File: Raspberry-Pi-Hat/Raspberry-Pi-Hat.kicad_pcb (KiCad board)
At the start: 4 copper layers, 65 x 56 mm, 127 parts, among them J1 Screw_Terminal_01x04, J2 Screw_Terminal_01x02, J3 40HAT, J4 Screw_Terminal_01x02, J5 USB_B, J6 CONN_02X02, J7 USB_A, J8 USB_A, J9 CONN_01X02, Q1 DMG2305UX, Q2 DMMT5401, U1 ADM3490ExR, U2 CAT24C32, U3 TCAN330, U4 LMZ13608, U5 TUSB4041I, U6 MCP2221AxSL, U7 MCP2221AxSL, U8 TPS2561, U9 TPS2561, Y1 24MHz

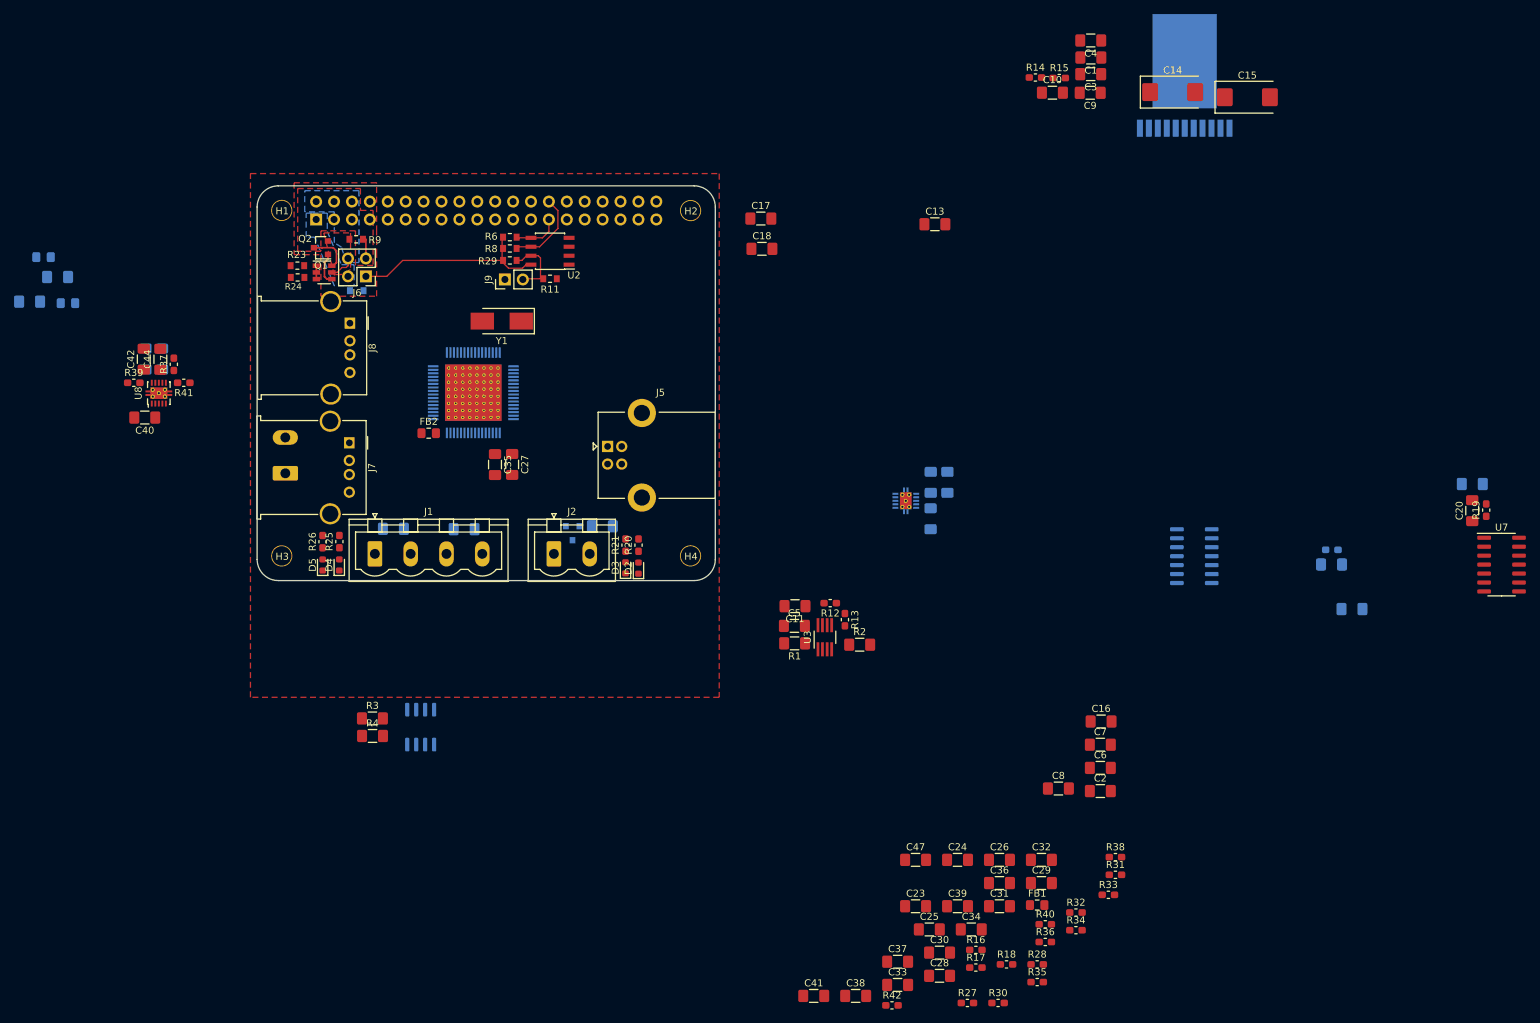
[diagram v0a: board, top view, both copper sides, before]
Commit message: Placed all component on board
All component placed on board.
Not many space left. Will probably reduce size of capacitors and resistors.
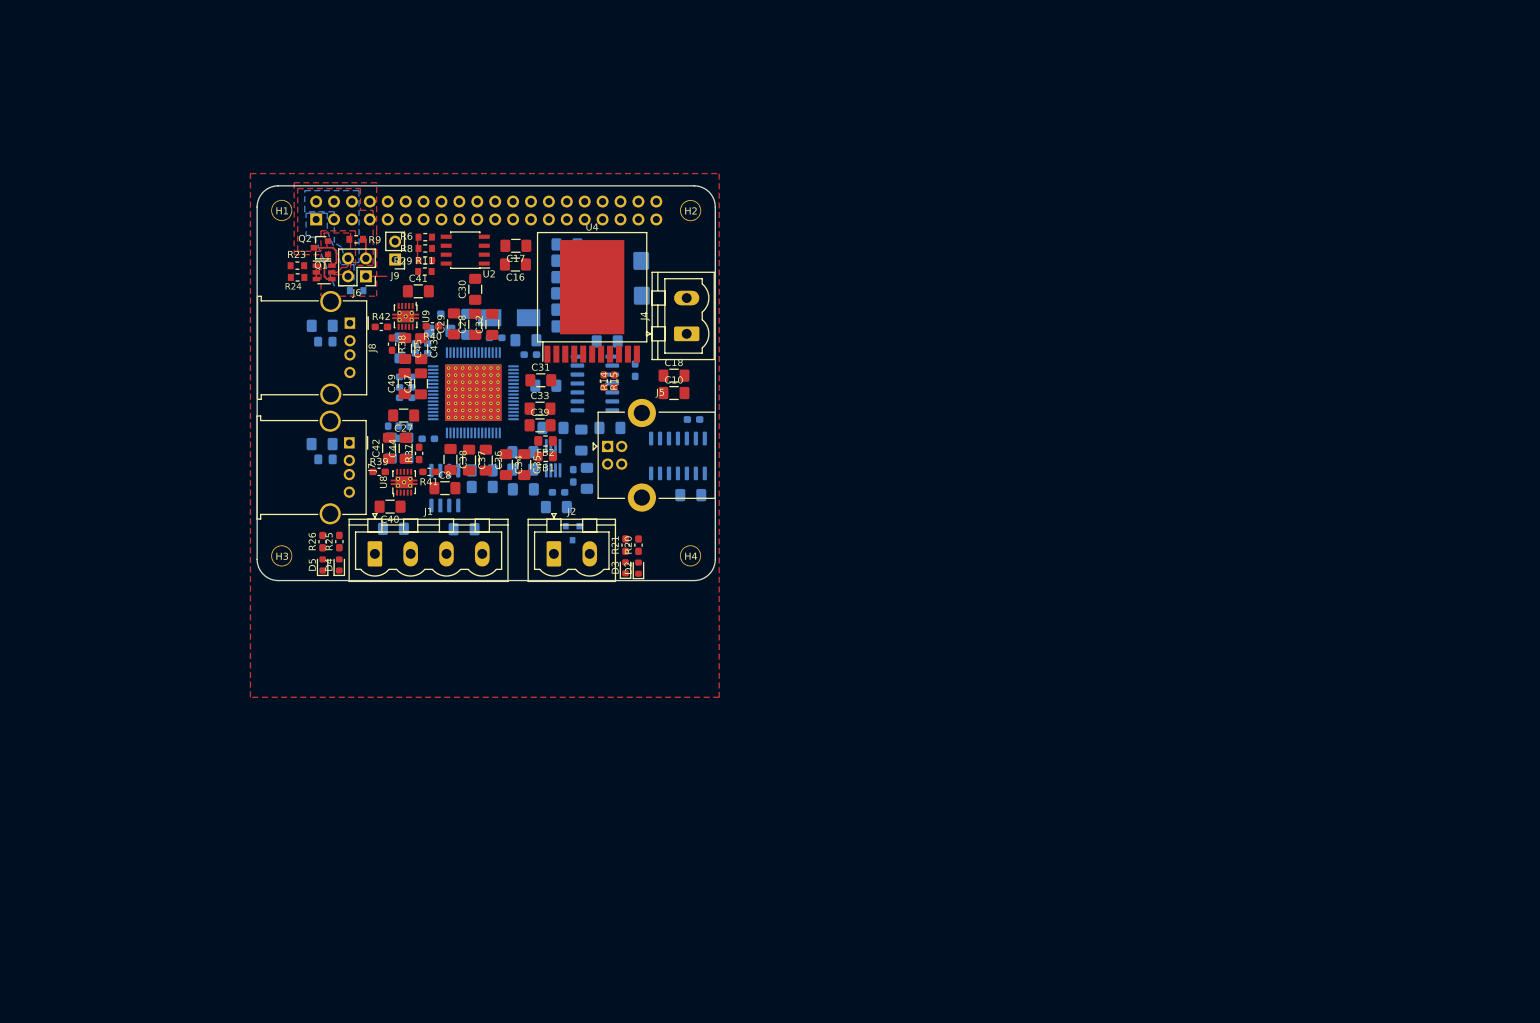
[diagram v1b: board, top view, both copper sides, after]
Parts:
- C1, C11, C13, C14, C15, C2, C20, C23, C24, C25, C26, C3, C4, C5, C6, C7, C9, R1, R12, R13, R16, R17, R18, R19, R2, R27, R28, R3, R30, R31, R32, R33, R34, R35, R36, R4, U3, U7, Y1: moved to B.Cu
- C43, C45, C49, J4, U4, U9: moved to F.Cu
- moved C20 132.6 mm to (119.5, 89.2), turned to 180 degrees
- moved R38 125.8 mm to (97.7, 83.3), turned to 270 degrees
- moved C19 124.4 mm to (128.2, 82.9)
- moved R32 123.2 mm to (105.5, 79.0)
- moved R31 123.0 mm to (99.6, 87.9), turned to 180 degrees
- moved R19 122.4 mm to (132.2, 87.0)
- moved R40 121.5 mm to (103.4, 80.7), turned to 180 degrees
- moved R33 121.4 mm to (97.1, 95.8), turned to 90 degrees
- moved R30 121.2 mm to (99.6, 89.4), turned to 180 degrees
- moved R42 120.5 mm to (96.2, 80.8)
- moved R18 120.0 mm to (101.9, 84.6)
- moved R34 119.3 mm to (98.6, 95.8), turned to 90 degrees
- moved R35 118.3 mm to (100.2, 95.8), turned to 90 degrees
- moved U7 117.9 mm to (138.2, 99.1), turned to 270 degrees
- moved R28 117.5 mm to (112.4, 82.4)
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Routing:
- net +3V3: track 28.5 -> 6.56 mm
- net /ID_SC_EEPROM: track 11.7 -> 0.61 mm
- net Net-(J9-Pad2): track 9.58 -> 0.30 mm
- net /ID_SD_EEPROM: track 7.43 -> 0.88 mm

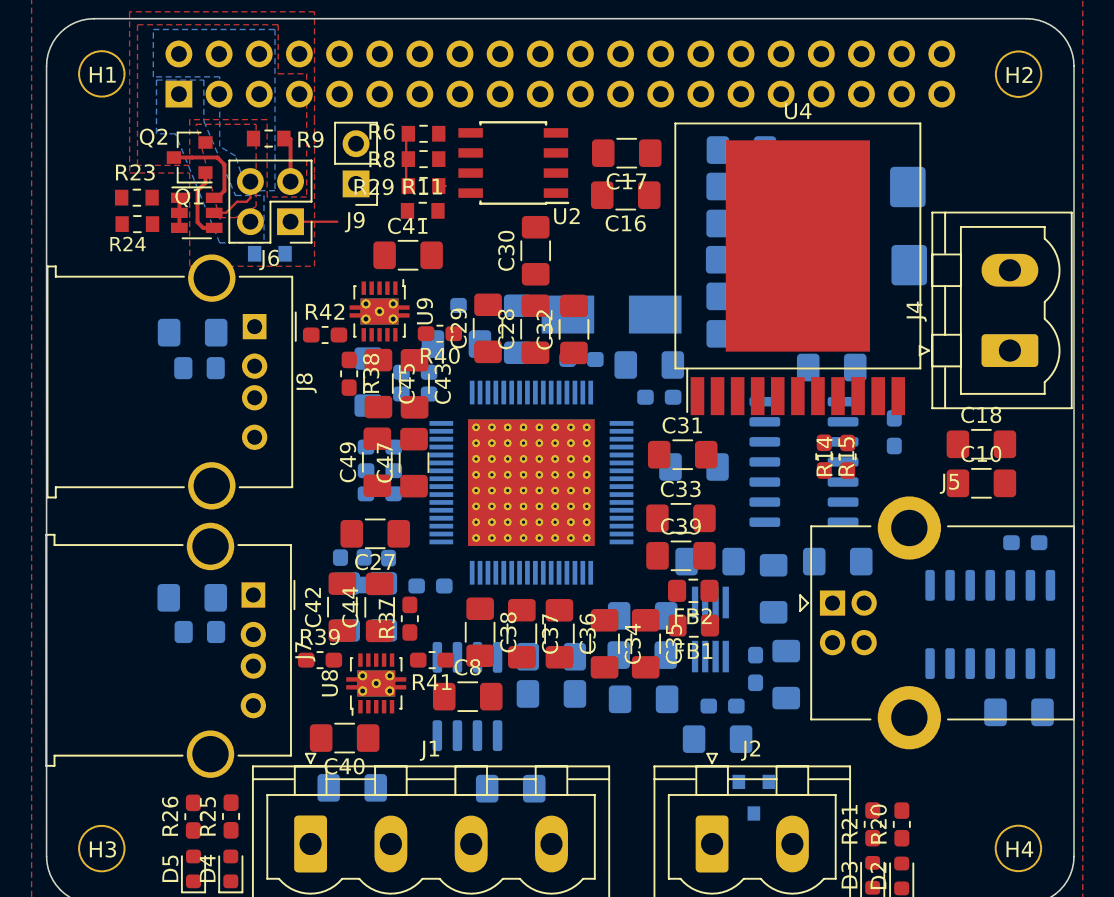
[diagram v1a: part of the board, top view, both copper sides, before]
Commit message: changed footprint size
changed resistor and capacitor footprint size for 0603 when possible.
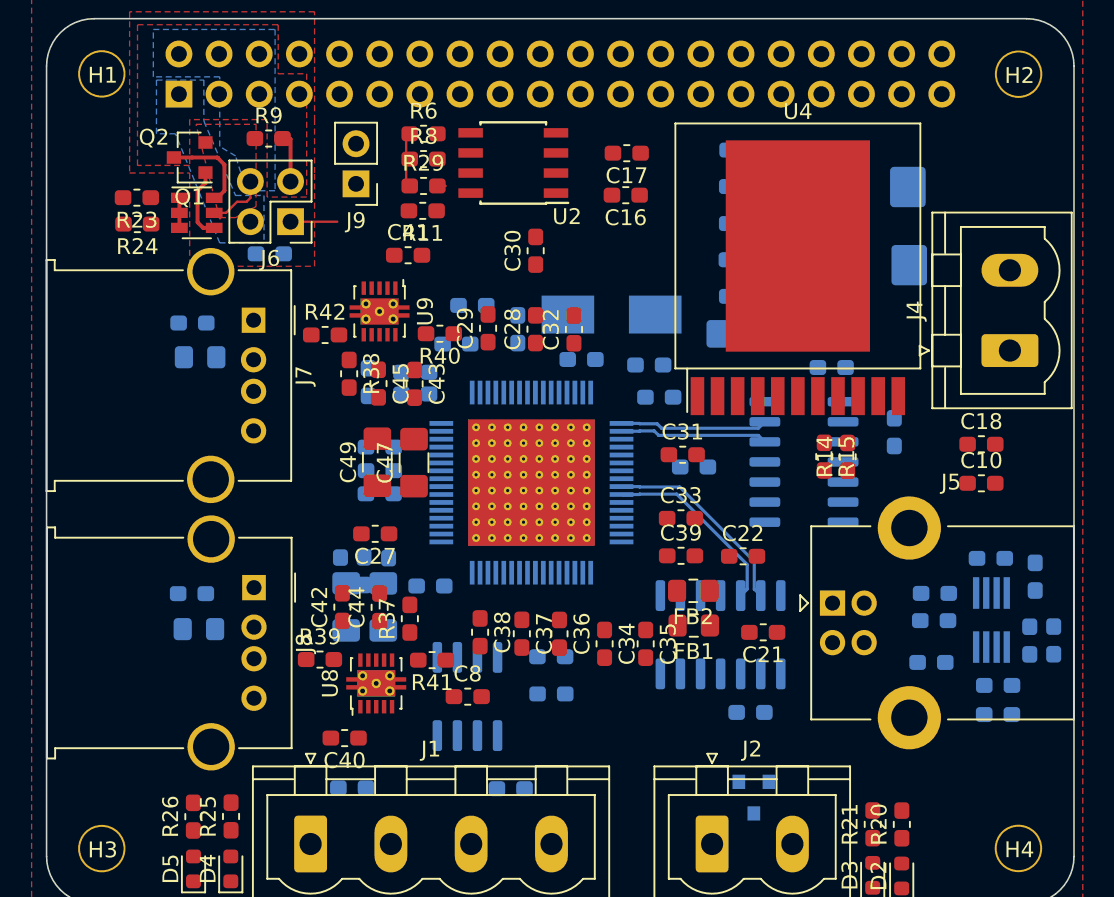
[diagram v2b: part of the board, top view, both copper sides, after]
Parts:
- C10, C11, C12, C13, C16, C17, C18, C19, C2, C20, C23, C24, C25, C26, C27, C28, C29, C3, C30, C31, C32, C33, C34, C35, C36, C37, C38, C39, C4, C40, C41, C42, C43, C44, C45, C5, C50, C51, C6, C7, C8, C9: footprint Capacitor_SMD:C_1206_3216Metric_Pad1.42x1.75mm_HandSolder -> Capacitor_SMD:C_0603_1608Metric_Pad1.05x0.95mm_HandSolder
- C21, C22: footprint Capacitor_SMD:C_1206_3216Metric_Pad1.42x1.75mm_HandSolder -> Capacitor_SMD:C_0603_1608Metric_Pad1.05x0.95mm_HandSolder; moved to F.Cu
- R1, R10, R2, R3, R4, R5: footprint Resistor_SMD:R_1206_3216Metric_Pad1.42x1.75mm_HandSolder -> Resistor_SMD:R_0603_1608Metric_Pad1.05x0.95mm_HandSolder
- R11, R23, R24, R29, R6, R7, R8, R9: footprint Resistor_SMD:R_0603_1608Metric_Pad0.84x1.00mm_HandSolder -> Resistor_SMD:R_0603_1608Metric_Pad1.05x0.95mm_HandSolder
- moved R22 20.4 mm to (123.1, 104.7), turned to 0 degrees
- moved C22 20.1 mm to (122.6, 94.8), turned to 0 degrees
- moved R13 18.9 mm to (142.3, 100.1)
- moved C5 18.9 mm to (134.7, 97.2)
- moved R1 18.4 mm to (134.7, 98.9)
- moved C11 18.4 mm to (134.5, 101.5)
- moved C13 17.8 mm to (138.7, 104.8)
- moved U3 17.8 mm to (138.3, 98.9)
- moved C7 17.8 mm to (138.3, 95.0)
- moved R12 17.5 mm to (138.7, 103.0)
- moved J7 17.4 mm to (91.6, 79.9)
- moved C50 17.4 mm to (87.8, 80.1)
- moved FB3 17.4 mm to (88.3, 82.2)
- moved U7 17.1 mm to (121.2, 99.8), turned to 90 degrees
- moved R2 16.6 mm to (141.1, 96.1)
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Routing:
- net USB_2_P: track 0.00 -> 12.7 mm
- net USB_2_N: track 0.00 -> 11.9 mm
- net USB_1_N: track 0.00 -> 9.36 mm
- net USB_1_P: track 0.00 -> 9.36 mm
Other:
- net class Default: clearance 0.2 -> 0.15
- net class Power added: clearance 0.15, trace_width 0.3, via_dia 0.4, via_drill 0.2
- rule trace_clearance: 0.2 -> 0.15
